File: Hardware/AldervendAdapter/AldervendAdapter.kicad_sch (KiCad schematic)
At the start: 40 parts, among them J101 MDB_MASTER, J102 MDB_SLAVE, J103 PROG, SW101 RESET, SW102 BOOT, U101 PC817, U102 PC817, U103 K7805M-1000R3, U104 AMS1117-3.3, U106 ESP32-C6-MINI-1

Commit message: Assign LCSC for THT parts
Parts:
- J101, J102: LSCS# (none) -> C114098
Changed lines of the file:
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@@
 			)
 		)
-		(property "LSCS#" ""
+		(property "LSCS#" "C114098"
 			(at 33.02 35.56 0)
 			(effects
@@
 			)
 		)
-		(property "LSCS#" ""
+		(property "LSCS#" "C114098"
 			(at 81.28 35.56 0)
 			(effects

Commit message: Last style
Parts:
- C101: footprint Capacitor_SMD:C_Elec_5x5.4 -> Capacitor_SMD:CP_Elec_6.3x5.4
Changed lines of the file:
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@@
 			)
 		)
-		(property "Footprint" "Capacitor_SMD:C_Elec_5x5.4"
+		(property "Footprint" "Capacitor_SMD:CP_Elec_6.3x5.4"
 			(at 26.67 125.73 0)
 			(effects

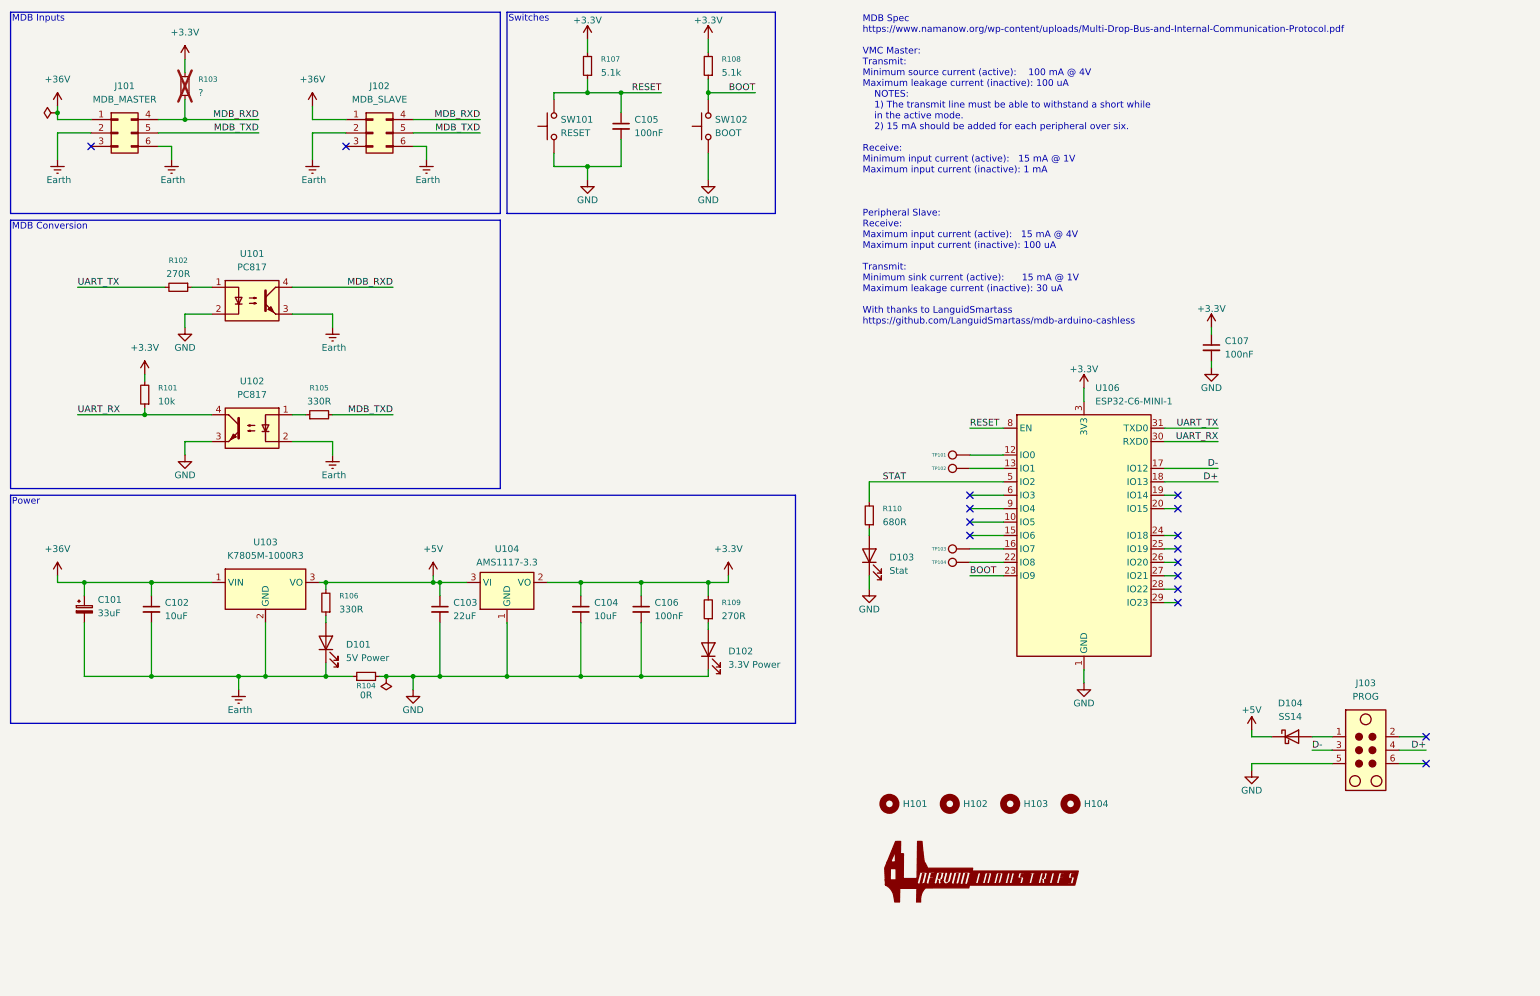
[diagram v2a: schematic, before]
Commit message: CLean sketch, finish fab (3d print)
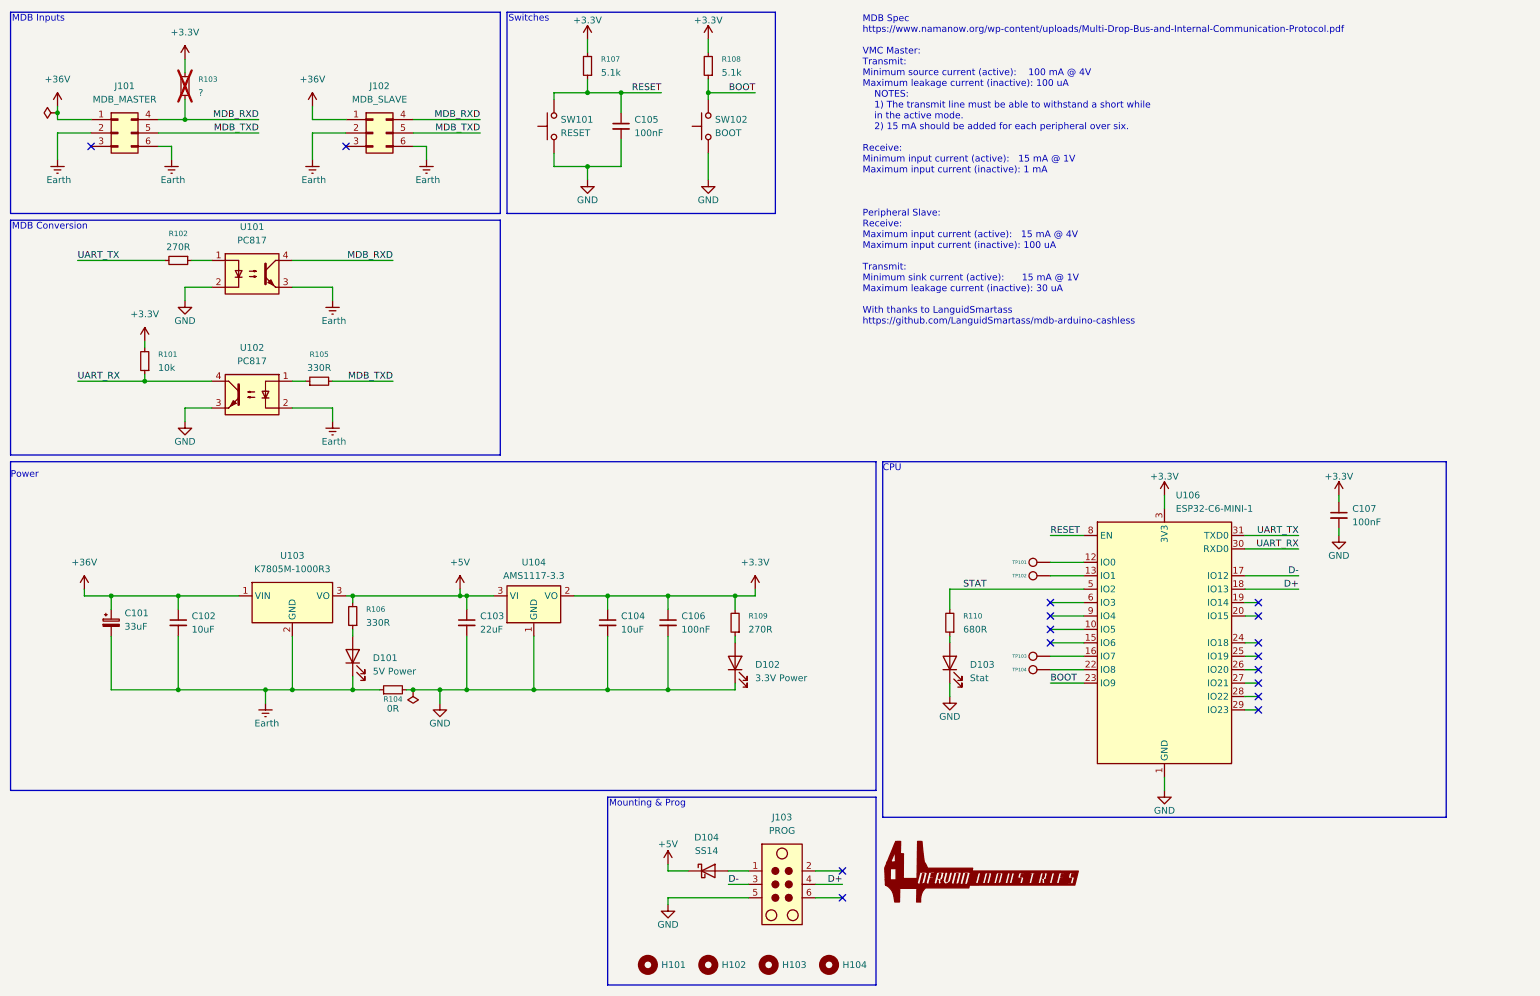
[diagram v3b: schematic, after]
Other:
- note added: "CPU"
- note added: "Mounting & Prog"
- moved on the sheet: C101, C102, C103, C104, C106, C107, D101, D102, D103, D104, H101, H102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

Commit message: Fix manufacturing width for iso
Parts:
- U101, U102: footprint Package_DIP:DIP-4_W7.62mm_SMDSocket_SmallPads -> Package_DIP:SMDIP-4_W9.53mm
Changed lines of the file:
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@@
 			)
 		)
-		(property "Footprint" "Package_DIP:DIP-4_W7.62mm_SMDSocket_SmallPads"
+		(property "Footprint" "Package_DIP:SMDIP-4_W9.53mm"
 			(at 63.5 90.17 0)
 			(effects
@@
 			)
 		)
-		(property "Footprint" "Package_DIP:DIP-4_W7.62mm_SMDSocket_SmallPads"
+		(property "Footprint" "Package_DIP:SMDIP-4_W9.53mm"
 			(at 53.34 67.31 0)
 			(effects
